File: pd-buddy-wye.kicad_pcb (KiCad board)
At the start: 2 copper layers, 20 x 25 mm, 7 parts, among them J1 Power, J2 UFP, P1 DFP+Power

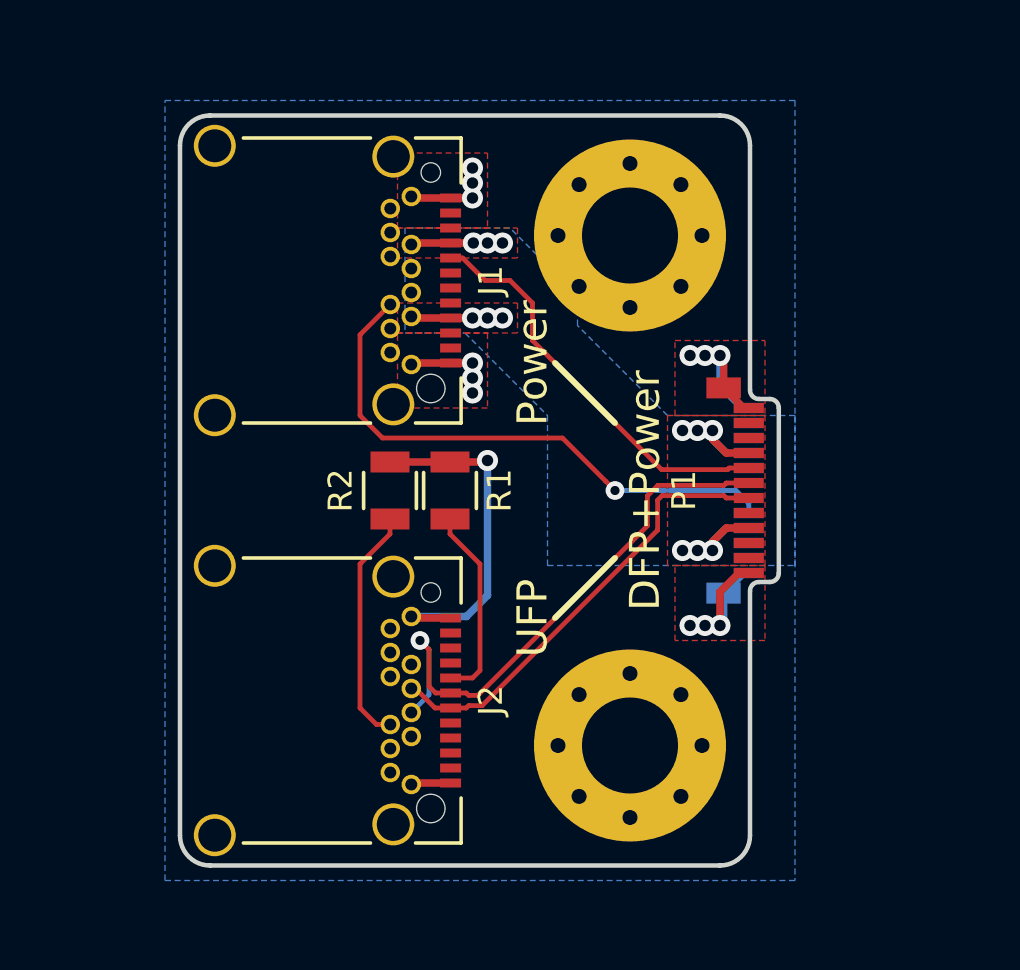
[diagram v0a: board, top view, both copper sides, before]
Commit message: v2.0: Use receptacles
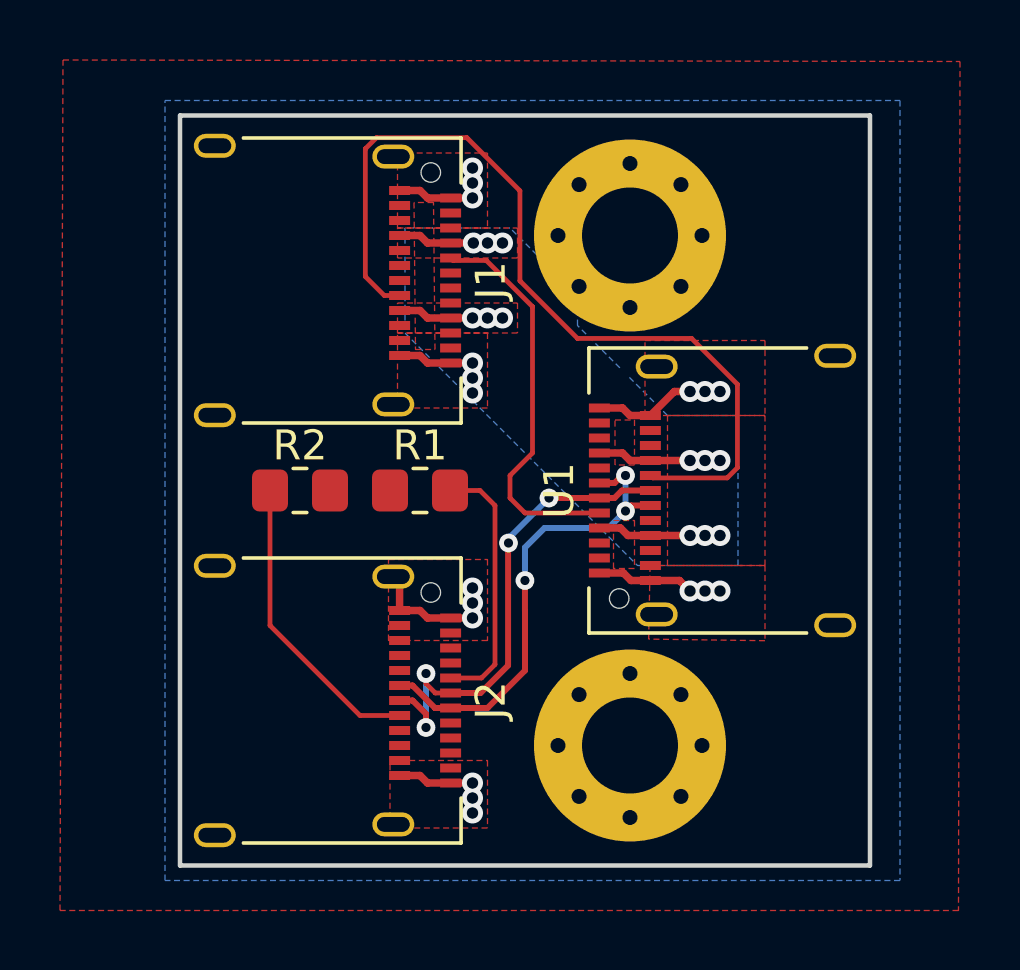
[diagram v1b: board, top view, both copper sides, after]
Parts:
- J1, J2: footprint Connectors_USB:USB_C_Receptacle_Amphenol_12401548E4-2A_CircularHoles -> Connector_USB:USB_C_Receptacle_Amphenol_12401610E4-2A
- MK1, MK2: footprint Mounting_Holes:MountingHole_3.2mm_M3_Pad_Via -> MountingHole:MountingHole_3.2mm_M3_Pad_Via
- R1, R2: footprint Resistors_SMD:R_0805 -> Resistor_SMD:R_0805_2012Metric_Pad1.20x1.40mm_HandSolder
- U1: renamed from P1; footprint Connectors_USB:USB_C_Plug_Molex_105444 -> Connector_USB:USB_C_Receptacle_Amphenol_12401610E4-2A
- moved R2 3.00 mm to (104.0, 112.5), turned to 180 degrees
- moved R1 1.00 mm to (108.0, 112.5), turned to 180 degrees
- turned U1 to 90 degrees
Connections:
- J1 pad A10: Net-(J1-PadA10) -> unconnected-(J1-RX2--PadA10)
- J1 pad A11: Net-(J1-PadA11) -> unconnected-(J1-RX2+-PadA11)
- J1 pad A2: Net-(J1-PadA2) -> unconnected-(J1-TX1+-PadA2)
- J1 pad A3: Net-(J1-PadA3) -> unconnected-(J1-TX1--PadA3)
- J1 pad A6: Net-(J1-PadA6) -> unconnected-(J1-D+-PadA6)
- J1 pad A7: Net-(J1-PadA7) -> unconnected-(J1-D--PadA7)
- J1 pad A8: Net-(J1-PadA8) -> unconnected-(J1-SBU1-PadA8)
- J1 pad B10: Net-(J1-PadB10) -> unconnected-(J1-RX1--PadB10)
- J1 pad B11: Net-(J1-PadB11) -> unconnected-(J1-RX1+-PadB11)
- J1 pad B2: Net-(J1-PadB2) -> unconnected-(J1-TX2+-PadB2)
- J1 pad B3: Net-(J1-PadB3) -> unconnected-(J1-TX2--PadB3)
- J1 pad B6: Net-(J1-PadB6) -> unconnected-(J1-D+-PadB6)
- J1 pad B7: Net-(J1-PadB7) -> unconnected-(J1-D--PadB7)
- J1 pad B8: Net-(J1-PadB8) -> unconnected-(J1-SBU2-PadB8)
- J2 pad A10: Net-(J2-PadA10) -> unconnected-(J2-RX2--PadA10)
- J2 pad A11: Net-(J2-PadA11) -> unconnected-(J2-RX2+-PadA11)
- J2 pad A2: Net-(J2-PadA2) -> unconnected-(J2-TX1+-PadA2)
- J2 pad A3: Net-(J2-PadA3) -> unconnected-(J2-TX1--PadA3)
- J2 pad A4: Net-(J2-PadA4) -> unconnected-(J2-VBUS-PadA4)
- J2 pad A8: Net-(J2-PadA8) -> unconnected-(J2-SBU1-PadA8)
- J2 pad A9: Net-(J2-PadA9) -> unconnected-(J2-VBUS-PadA9)
- J2 pad B10: Net-(J2-PadB10) -> unconnected-(J2-RX1--PadB10)
- J2 pad B11: Net-(J2-PadB11) -> unconnected-(J2-RX1+-PadB11)
- J2 pad B2: Net-(J2-PadB2) -> unconnected-(J2-TX2+-PadB2)
- J2 pad B3: Net-(J2-PadB3) -> unconnected-(J2-TX2--PadB3)
- J2 pad B4: Net-(J2-PadB4) -> unconnected-(J2-VBUS-PadB4)
- J2 pad B8: Net-(J2-PadB8) -> unconnected-(J2-SBU2-PadB8)
- J2 pad B9: Net-(J2-PadB9) -> unconnected-(J2-VBUS-PadB9)
- U1 pad A10: Net-(P1-PadA10) -> unconnected-(U1-RX2--PadA10)
- U1 pad A11: Net-(P1-PadA11) -> unconnected-(U1-RX2+-PadA11)
- U1 pad A2: Net-(P1-PadA2) -> unconnected-(U1-TX1+-PadA2)
- U1 pad A3: Net-(P1-PadA3) -> unconnected-(U1-TX1--PadA3)
- U1 pad A8: Net-(P1-PadA8) -> unconnected-(U1-SBU1-PadA8)
- U1 pad B10: Net-(P1-PadB10) -> unconnected-(U1-RX1--PadB10)
- U1 pad B11: Net-(P1-PadB11) -> unconnected-(U1-RX1+-PadB11)
- U1 pad B2: Net-(P1-PadB2) -> unconnected-(U1-TX2+-PadB2)
- U1 pad B3: Net-(P1-PadB3) -> unconnected-(U1-TX2--PadB3)
- U1 pad B8: Net-(P1-PadB8) -> unconnected-(U1-SBU2-PadB8)
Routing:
- net /CC2P: track 18.6 -> 29.2 mm, vias 1 -> 0
- net GND: track 30.5 -> 23.3 mm, vias 13 -> 18
- net /CC1D: track 6.55 -> 8.67 mm
- net /CC2D: track 7.95 -> 10.1 mm
- net /D+: track 18.7 -> 16.7 mm, vias 1 -> 4
- net /D-: track 15.1 -> 16.0 mm, vias 0 -> 3
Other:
- board size 20 x 25 mm -> 23 x 25 mm
- net class Default removed
- net class Power removed
- net class Power_Small removed
- board text added: "PD Buddy Wye v2.0 AK"
- board text removed: "PD Buddy Wye v1.1"
